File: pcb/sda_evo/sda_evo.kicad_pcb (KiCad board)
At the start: 4 copper layers, 61.5 x 106.7 mm, 138 parts, among them J1 PROG, J10 SPKR, J11 AudioJack, J2 USB_C_Receptacle_USB2.0, J3 Conn_01x40, J4 INT_EXP, J5 BATT, J9 Micro_SD_Card_Det, Q1 IRLML6302, SW1 RESET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

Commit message: did some stuff
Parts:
- added C54: 100n, Capacitor_SMD:C_0805_2012Metric_Pad1.18x1.45mm_HandSolder, B.Cu at (77.3, 69.6)
- added C55: 1u, Capacitor_SMD:C_0805_2012Metric_Pad1.18x1.45mm_HandSolder, B.Cu at (77.2, 72.4)
- added C56: 100n, Capacitor_SMD:C_0805_2012Metric_Pad1.18x1.45mm_HandSolder, B.Cu at (112.6, 101.5)
- added C57: 2.2u, Capacitor_SMD:C_0805_2012Metric_Pad1.18x1.45mm_HandSolder, B.Cu at (112.6, 99.4)
- added C58: 390n, Capacitor_SMD:C_0805_2012Metric_Pad1.18x1.45mm_HandSolder, B.Cu at (64.5, 70.5)
- added C59: 390n, Capacitor_SMD:C_0805_2012Metric_Pad1.18x1.45mm_HandSolder, F.Cu at (62.4, 62.9)
- added C60: 390n, Capacitor_SMD:C_0805_2012Metric_Pad1.18x1.45mm_HandSolder, F.Cu at (62.4, 64.9)
- added R31: 20k, Resistor_SMD:R_0805_2012Metric_Pad1.20x1.40mm_HandSolder, B.Cu at (64.5, 74.6)
- added R32: 20k, Resistor_SMD:R_0805_2012Metric_Pad1.20x1.40mm_HandSolder, F.Cu at (62.4, 68.9)
- added R33: 10k, Resistor_SMD:R_0805_2012Metric_Pad1.20x1.40mm_HandSolder, B.Cu at (110.3, 70.5)
- added R34: R_Photo, LED_THT:LED_D5.0mm, F.Cu at (110.7, 56.7)
- added R35: 20k, Resistor_SMD:R_0805_2012Metric_Pad1.20x1.40mm_HandSolder, B.Cu at (64.5, 72.6)
- added R36: 20k, Resistor_SMD:R_0805_2012Metric_Pad1.20x1.40mm_HandSolder, F.Cu at (62.4, 66.9)
- added TP6: AUX_SW, TestPoint:TestPoint_Pad_D2.5mm, F.Cu at (109.5, 104.4)
- added TP7: AUX_GND, TestPoint:TestPoint_Pad_D2.5mm, F.Cu at (109.5, 109.7)
- added TP8: PD3, TestPoint:TestPoint_Pad_D2.5mm, B.Cu at (113.8, 76.9)
- added TP9: PD4, TestPoint:TestPoint_Pad_D2.5mm, B.Cu at (113.8, 80.5)
- added U12: AP22802AW5-7, Package_TO_SOT_SMD:SOT-23-5_HandSoldering, B.Cu at (112.0, 104.6)
- added U13: ~, Package_SO:HSOP-8-1EP_3.9x4.9mm_P1.27mm_EP2.41x3.1mm, B.Cu at (71.1, 73.0)
- C22, C23: value 12,5p -> 15p
- C3, C4: value 12p -> 15p
- C30, C32, C35, C36, C37, C38, C40, C42, C43, C44, C45, C47, R24, R25, U7: moved to F.Cu
- C48: value ?? -> 660p ?
- moved R25 18.9 mm to (80.5, 65.0)
- moved C45 18.8 mm to (80.5, 67.2), turned to 0 degrees
- moved R24 18.8 mm to (80.5, 71.4), turned to 0 degrees
- moved C47 18.8 mm to (80.5, 69.2), turned to 0 degrees
- moved C40 18.0 mm to (80.4, 76.9), turned to 0 degrees
- moved C36 17.7 mm to (80.5, 73.4), turned to 0 degrees
- moved C38 17.4 mm to (62.4, 73.2), turned to 180 degrees
- moved C43 17.4 mm to (62.4, 71.2), turned to 180 degrees
- moved C32 17.4 mm to (62.4, 75.3), turned to 180 degrees
- moved C30 17.4 mm to (62.4, 77.3), turned to 180 degrees
- moved C42 15.3 mm to (76.7, 80.8), turned to 0 degrees
- moved C44 15.3 mm to (76.7, 82.9), turned to 0 degrees
- moved R30 14.3 mm to (77.2, 74.4), turned to 0 degrees
- moved C35 6.99 mm to (65.2, 82.9), turned to 180 degrees
- moved C37 6.95 mm to (65.3, 80.8), turned to 180 degrees
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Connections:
- J10 pad 2: GNDA -> Net-(J10-Pin_2)
- J11 pad RN: Net-(J10-Pin_1) -> Net-(C59-Pad1)
- J11 pad TN: Net-(J10-Pin_1) -> Net-(C60-Pad1)
- U10 pad 1: unconnected-(U10-PE2-Pad1) -> AUX_SWITCH
- U10 pad 114: unconnected-(U10-PD0-Pad114) -> Net-(U10-PD0)
- U10 pad 115: unconnected-(U10-PD1-Pad115) -> Net-(U10-PD1)
- U10 pad 27: BTN_A -> BTN_RIGHT
- U10 pad 40: unconnected-(U10-PA4-Pad40) -> AMB_SENS
- U10 pad 45: BTN_RIGHT -> BTN_A
- U10 pad 85: IEXP2_P9 -> BEEPER
- U10 pad 86: IEXP2_P10 -> SPKR_SHDN
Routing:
- net AMB_SENS: track 0.00 -> 71.8 mm, vias 0 -> 2
- net +5V: track 50.8 -> 106.8 mm, vias 2 -> 4
- net BEEPER: track 0.00 -> 41.8 mm, vias 0 -> 2
- net SPKR_SHDN: track 0.00 -> 27.7 mm, vias 0 -> 2
- net GND: track 199.2 -> 222.5 mm, vias 68 -> 64
- net Net-(J10-Pin_2): track 0.00 -> 21.1 mm, vias 0 -> 1
- net PCM_SD: track 33.5 -> 53.4 mm
- net PCM_MUTE: track 33.4 -> 49.7 mm
- net BTN_A: track 87.2 -> 71.6 mm
- net Net-(C45-Pad1): track 9.17 -> 24.8 mm, vias 0 -> 1
- net Net-(C59-Pad1): track 0.00 -> 13.8 mm, vias 0 -> 1
- net +3V3: track 459.5 -> 473.1 mm, vias 18 -> 16
- net AUX_SWITCH: track 0.00 -> 12.7 mm
- net Net-(U12-OUT): track 0.00 -> 12.2 mm, vias 0 -> 1
- net Net-(U10-PD0): track 0.00 -> 9.58 mm
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- added copper zone on B.Cu, net GNDA
- added copper zone on F.Cu, net GNDA
- added copper zone on In1.Cu, net GNDA
- added copper zone on In2.Cu, net GNDA

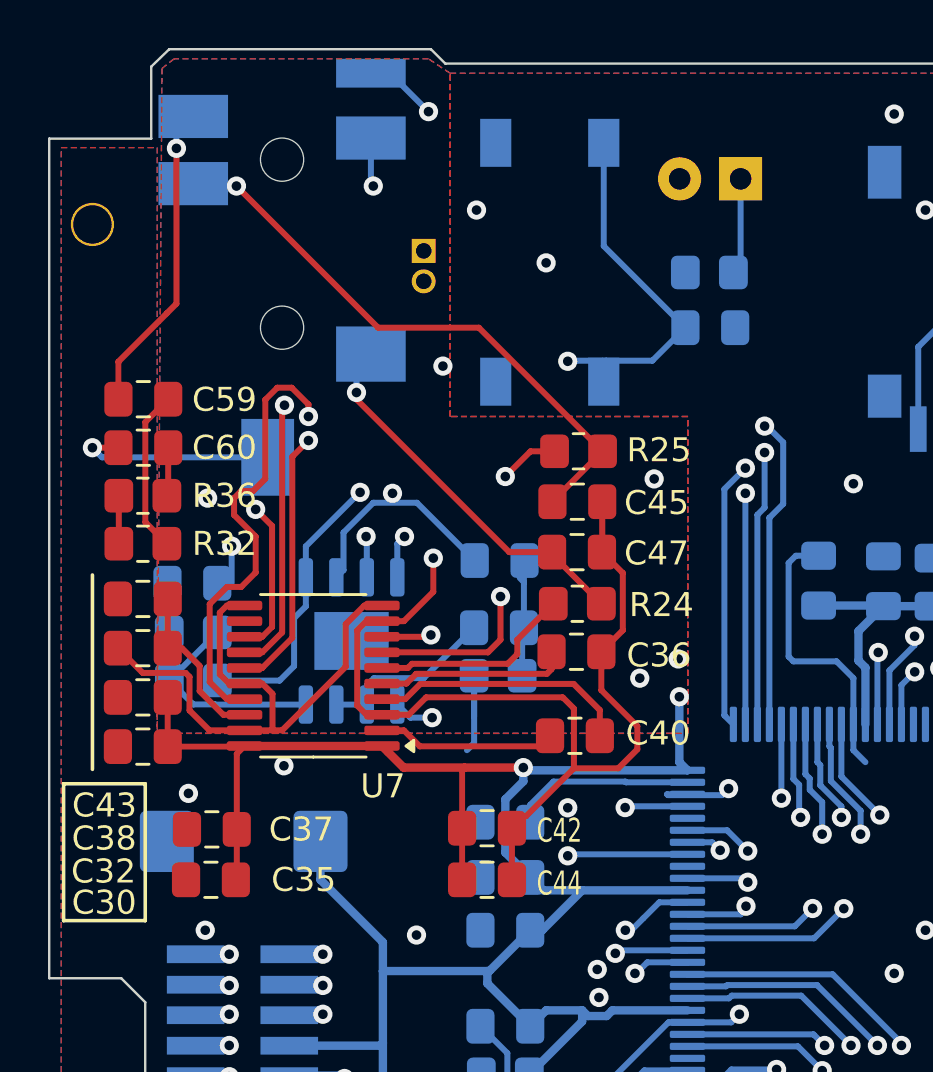
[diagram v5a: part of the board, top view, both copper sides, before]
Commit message: pcb: dac turned around
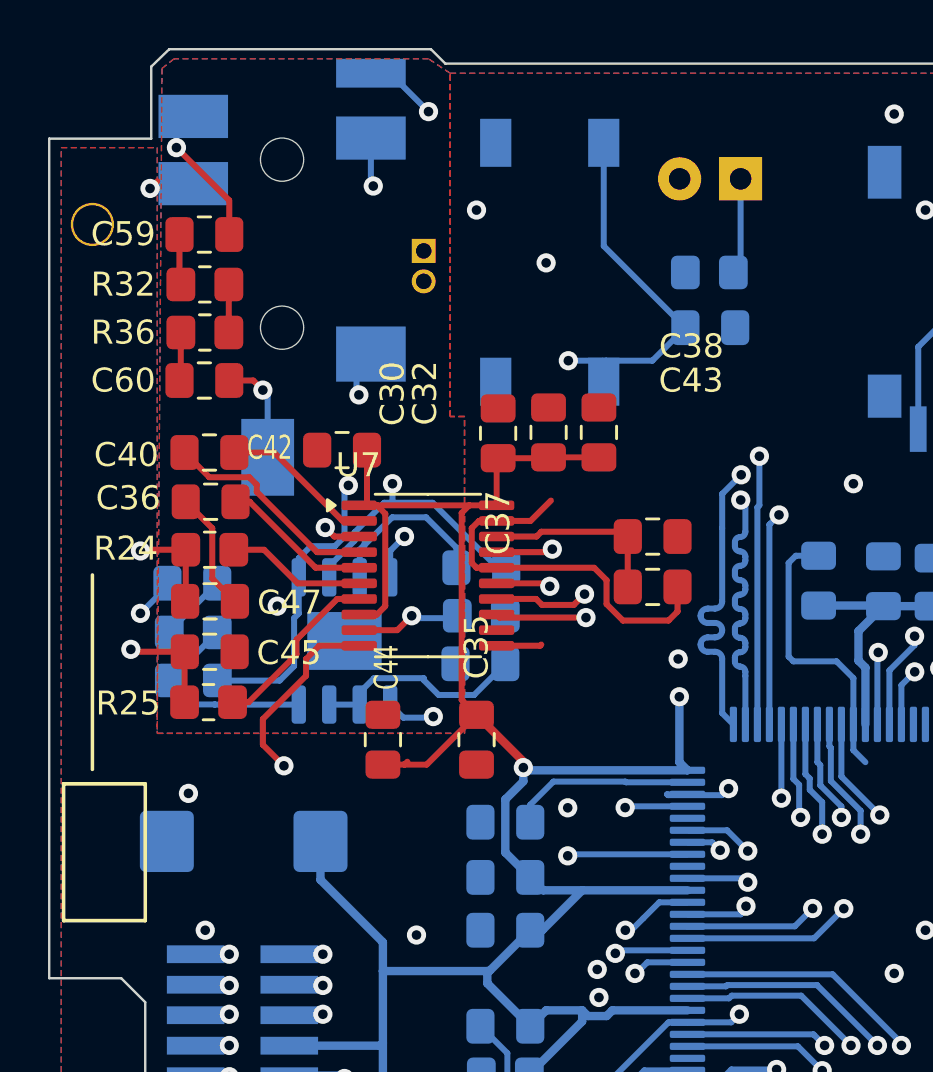
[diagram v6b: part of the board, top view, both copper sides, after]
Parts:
- moved C32 22.0 mm to (81.4, 64.3), turned to 90 degrees
- moved C38 21.7 mm to (83.6, 68.6), turned to 0 degrees
- moved C30 21.4 mm to (79.3, 64.3), turned to 90 degrees
- moved C43 21.2 mm to (83.6, 70.7), turned to 0 degrees
- moved C37 20.4 mm to (77.2, 64.3), turned to 90 degrees
- moved C40 19.3 mm to (65.2, 65.1), turned to 180 degrees
- moved R25 18.6 mm to (65.1, 75.5), turned to 180 degrees
- moved C42 16.9 mm to (70.7, 65.0), turned to 180 degrees
- moved C45 16.5 mm to (65.2, 73.4)
- moved C36 16.5 mm to (65.2, 67.2), turned to 180 degrees
- moved R24 15.5 mm to (65.2, 69.2), turned to 180 degrees
- moved C47 15.4 mm to (65.2, 71.3)
- moved C35 12.5 mm to (76.3, 77.1), turned to -90 degrees
- moved R32 11.1 mm to (65.0, 58.1), turned to 0 degrees
- moved C59 7.32 mm to (65.0, 56.0), turned to 180 degrees
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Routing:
- net GNDA: track 65.5 -> 20.6 mm, vias 6 -> 4
- net PCM_SD: track 53.4 -> 25.7 mm
- net PCM_MUTE: track 49.7 -> 23.8 mm
- net PCM_WS: track 40.9 -> 25.6 mm
- net PCM_CK: track 37.0 -> 25.5 mm
- net Net-(U7-OUTR): track 14.5 -> 7.41 mm, vias 2 -> 0
- net Net-(C59-Pad1): track 13.8 -> 6.86 mm
- net Net-(C59-Pad2): track 6.79 -> 2.10 mm
- net Net-(C60-Pad1): track 8.55 -> 4.45 mm
- net Net-(U7-OUTL): track 8.60 -> 5.80 mm
- net GND: track 222.5 -> 219.8 mm, vias 64 -> 63
- net +5V: track 106.8 -> 109.3 mm
- net Net-(C47-Pad1): track 15.9 -> 18.3 mm, vias 1 -> 2
- net Net-(C45-Pad1): track 24.8 -> 26.6 mm, vias 1 -> 2
- net Net-(U7-VNEG): track 8.04 -> 6.29 mm
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
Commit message: repo cleanup, board twaked
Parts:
- removed R30: 0, Resistor_SMD:R_0805_2012Metric_Pad1.20x1.40mm_HandSolder
- C48: value 660p ? -> 680p ?
- J3: value Conn_01x40 -> LCD_CONN
- U13: value ~ -> LM4861
- moved R34 10.8 mm to (116.2, 66.0), turned to 90 degrees
- moved J5 2.16 mm to (65.0, 136.4), turned to 180 degrees
- moved J9 1.08 mm to (104.5, 50.1)
- moved F1 0.80 mm to (69.2, 135.8)
- moved Q1 0.70 mm to (69.5, 139.4)
- turned C54 to 0 degrees
- turned C55 to 0 degrees
- turned H1 to 180 degrees
- renumbered IEXP1 to EXP1
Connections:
- C36 pad 2: GNDA -> GND
- C42 pad 2: GNDA -> GND
- C44 pad 2: GNDA -> GND
- C45 pad 2: GNDA -> GND
- C47 pad 2: GNDA -> GND
- C54 pad 2: GNDA -> GND
- C55 pad 2: GNDA -> GND
- J11 pad S: GNDA -> GND
- U13 pad 7: GNDA -> GND
- U7 pad 3: GNDA -> GND
- U7 pad 9: GNDA -> GND
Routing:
- net GND: track 219.8 -> 244.8 mm, vias 63 -> 67
- net GNDA: track 20.6 -> 0.00 mm, vias 4 -> 0
- net AMB_SENS: track 71.8 -> 65.1 mm
- net +3V3: track 473.7 -> 478.2 mm
- net Net-(U13-+IN): track 9.36 -> 6.26 mm
- net SD_CLK: track 35.0 -> 32.1 mm
- net VBUS: track 91.6 -> 93.7 mm
- net Net-(J2-D+-PadA6): track 23.2 -> 21.4 mm
- net VD: track 68.3 -> 69.8 mm
- net +BATT: track 83.7 -> 82.5 mm
- net SD_D0: track 35.8 -> 36.9 mm
- net SD_DETECT: track 38.6 -> 39.7 mm
- net +5V: track 109.3 -> 108.2 mm
- net BEEPER: track 40.1 -> 39.2 mm
- net Net-(J2-D--PadA7): track 24.9 -> 24.1 mm
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- removed copper zone on B.Cu, net GNDA
- removed copper zone on F.Cu, net GNDA
- removed copper zone on In1.Cu, net GNDA
- removed copper zone on In2.Cu, net GNDA
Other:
- board size 61.5 x 106.7 mm -> 61.5 x 105.9 mm
- board text added: "Beta 0 V. 2025 Designed in Budweis by Standa"
- board text removed: "Beta 0 V. 2024 Designed in Budweis by Standa"
